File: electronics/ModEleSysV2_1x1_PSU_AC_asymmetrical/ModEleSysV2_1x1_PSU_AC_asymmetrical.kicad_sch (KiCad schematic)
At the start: 38 parts, among them J2 Jack-DC, SW1 switch_DPDT, U1 LM317, U2 LM337

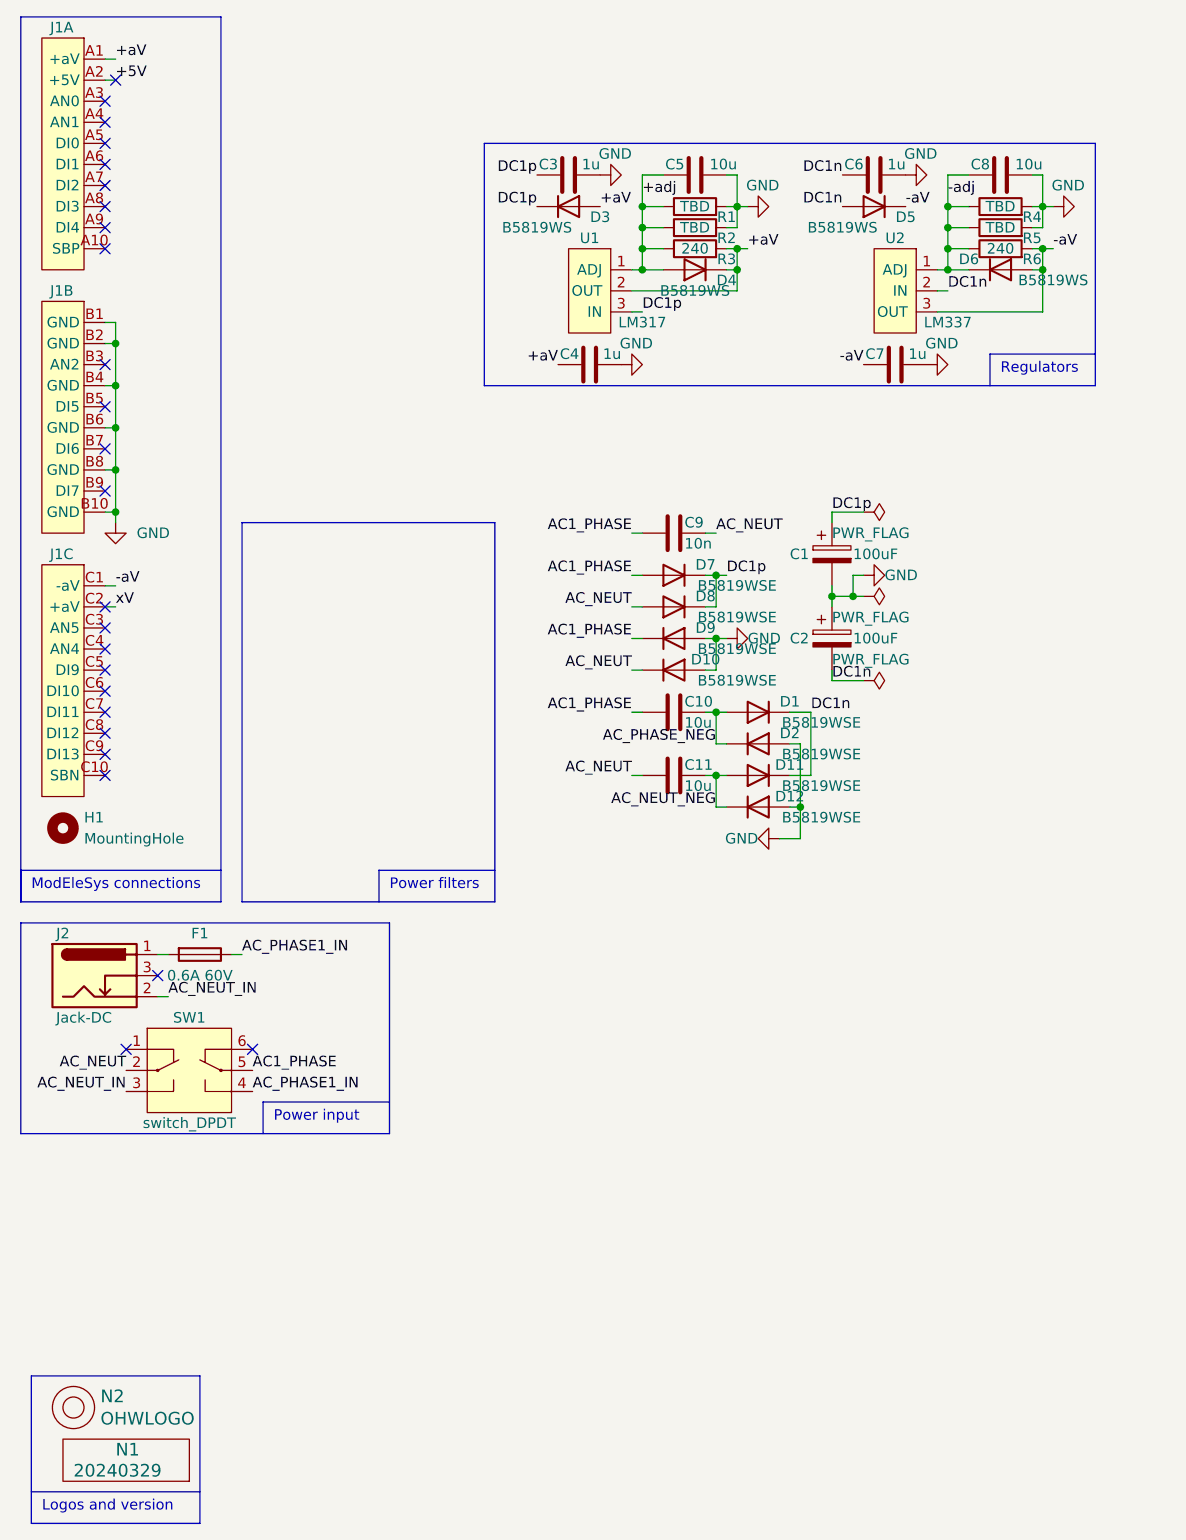
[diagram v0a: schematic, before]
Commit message: added second regulator
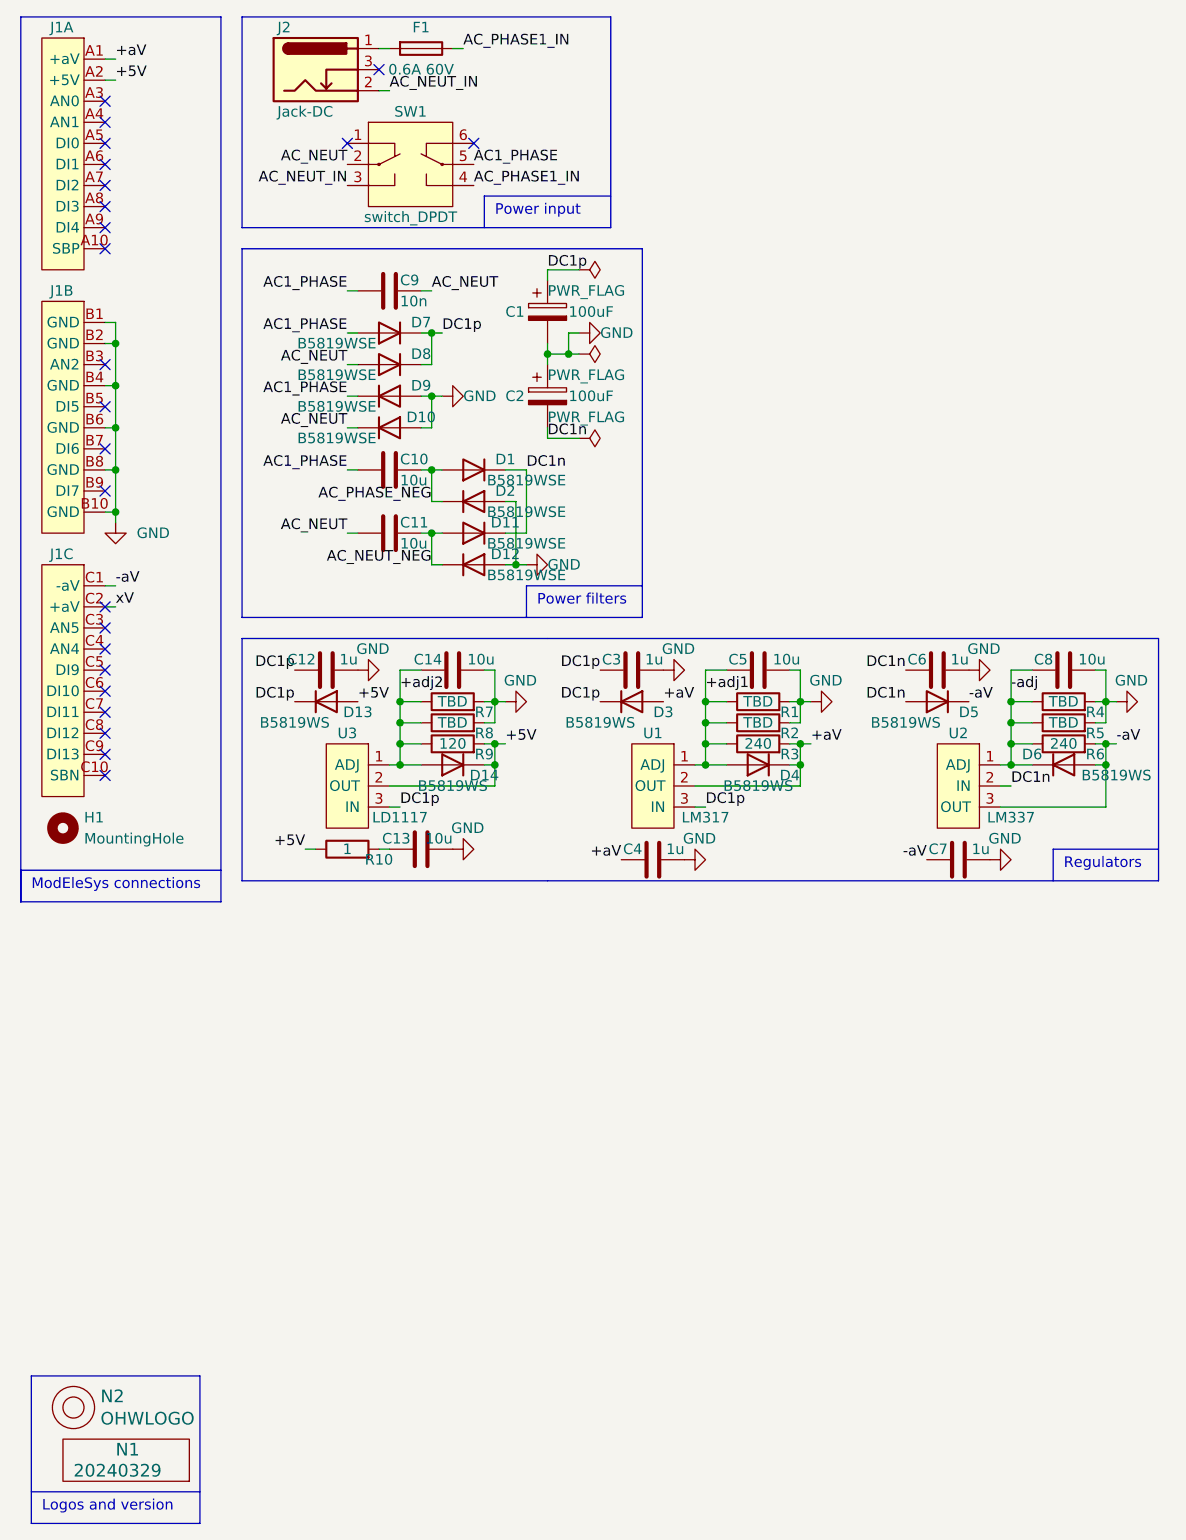
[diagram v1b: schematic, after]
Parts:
- added C12: 1u, SquantorCapacitor:C_0805+0603, symbol Device:C
- added C13: 10u, SquantorCapacitor:C_1206_0805, symbol Device:C
- added C14: 10u, SquantorCapacitor:C_0805+0603, symbol Device:C
- added D13, D14: B5819WS, SquantorDiodes:SOD-323HE-shikues, symbol Device:D
- added R10: 1, SquantorResistor:R_0603_hand, symbol Device:R
- added R7, R8: TBD, SquantorResistor:R_0603_hand, symbol Device:R
- added R9: 120, SquantorResistor:R_0603_hand, symbol Device:R
- added U3: LD1117, SquantorIC:TO-252_D-PAK_IRF, symbol SquantorGenericAnalog:LM317
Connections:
- net +5V: now also D13.2 (A), D14.1 (K), R10.1, R9.2, U3.2 (OUT)
- net DC1p: now also C12.1, D13.1 (K), U3.3 (IN)
- net GND: now also C12.2, C13.2, C14.2, R7.2, R8.2
- net +adj renamed +adj1
- new net: C13.1, R10.2
- new net +adj2: C14.1, D14.2 (A), R7.1, R8.1, R9.1, U3.1 (ADJ)
- no-connect marks 25 -> 24
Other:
- moved on the sheet: C1, C10, C11, C2, C3, C4, C5, C6, C7, C8, C9, D1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

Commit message: silk placement done
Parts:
- R10: value 1 -> 1R
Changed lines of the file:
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@@
       (effects (font (size 1.27 1.27)))
     )
-    (property "Value" "1" (at 53.34 114.3 90)
+    (property "Value" "1R" (at 53.34 114.3 90)
       (effects (font (size 1.27 1.27)))
     )

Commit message: reviewed
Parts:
- C4, C7: footprint SquantorCapacitor:C_0805+0603 -> SquantorCapacitor:C_1206_0805
- N1: value 20240329 -> 20240424
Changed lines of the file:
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@@
       (effects (font (size 1.524 1.524)) (justify left))
     )
-    (property "Value" "20240329" (at 20.32 189.23 0)
+    (property "Value" "20240424" (at 20.32 189.23 0)
       (effects (font (size 1.524 1.524)) (justify left))
     )
@@
       (effects (font (size 1.27 1.27)) (justify left))
     )
-    (property "Footprint" "SquantorCapacitor:C_0805+0603" (at 93.98 114.6048 0)
+    (property "Footprint" "SquantorCapacitor:C_1206_0805" (at 93.98 114.6048 0)
       (effects (font (size 1.27 1.27)) hide)
     )
@@
       (effects (font (size 1.27 1.27)) (justify left))
     )
-    (property "Footprint" "SquantorCapacitor:C_0805+0603" (at 130.81 114.6048 0)
-      (effects (font (size 1.27 1.27)) hide)
-    )
+    (property "Footprint" "SquantorCapacitor:C_1206_0805" (at 130.81 114.6048 0)
+      (effects (font (size 1.27 1.27)) hide)
+    )

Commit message: updated versionnumbers
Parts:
- N1: value 20240424 -> 20240426
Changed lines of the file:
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@@
       (effects (font (size 1.524 1.524)) (justify left))
     )
-    (property "Value" "20240424" (at 20.32 189.23 0)
+    (property "Value" "20240426" (at 20.32 189.23 0)
       (effects (font (size 1.524 1.524)) (justify left))
     )
